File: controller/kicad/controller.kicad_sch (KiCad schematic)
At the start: 40 parts, among them J1 pcie_98, J2 USB_C_Receptacle_USB2.0, SW1 SW_MEC_5E, U1 WeAct_STM32H750_Module, U10 ESD5344D, U11 ESD5344D, U12 ESD5344D, U13 ESD5344D, U14 ESD5344D, U15 ESD5344D, U16 CP2102N-A01-GQFN28-Interface_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, U2 ESD5344D, U3 ESD5344D, U4 ESD5344D, U5 ESD5344D, U6 ESD5344D, U7 ESD5344D, U8 ESD5344D, U9 ESD5344D

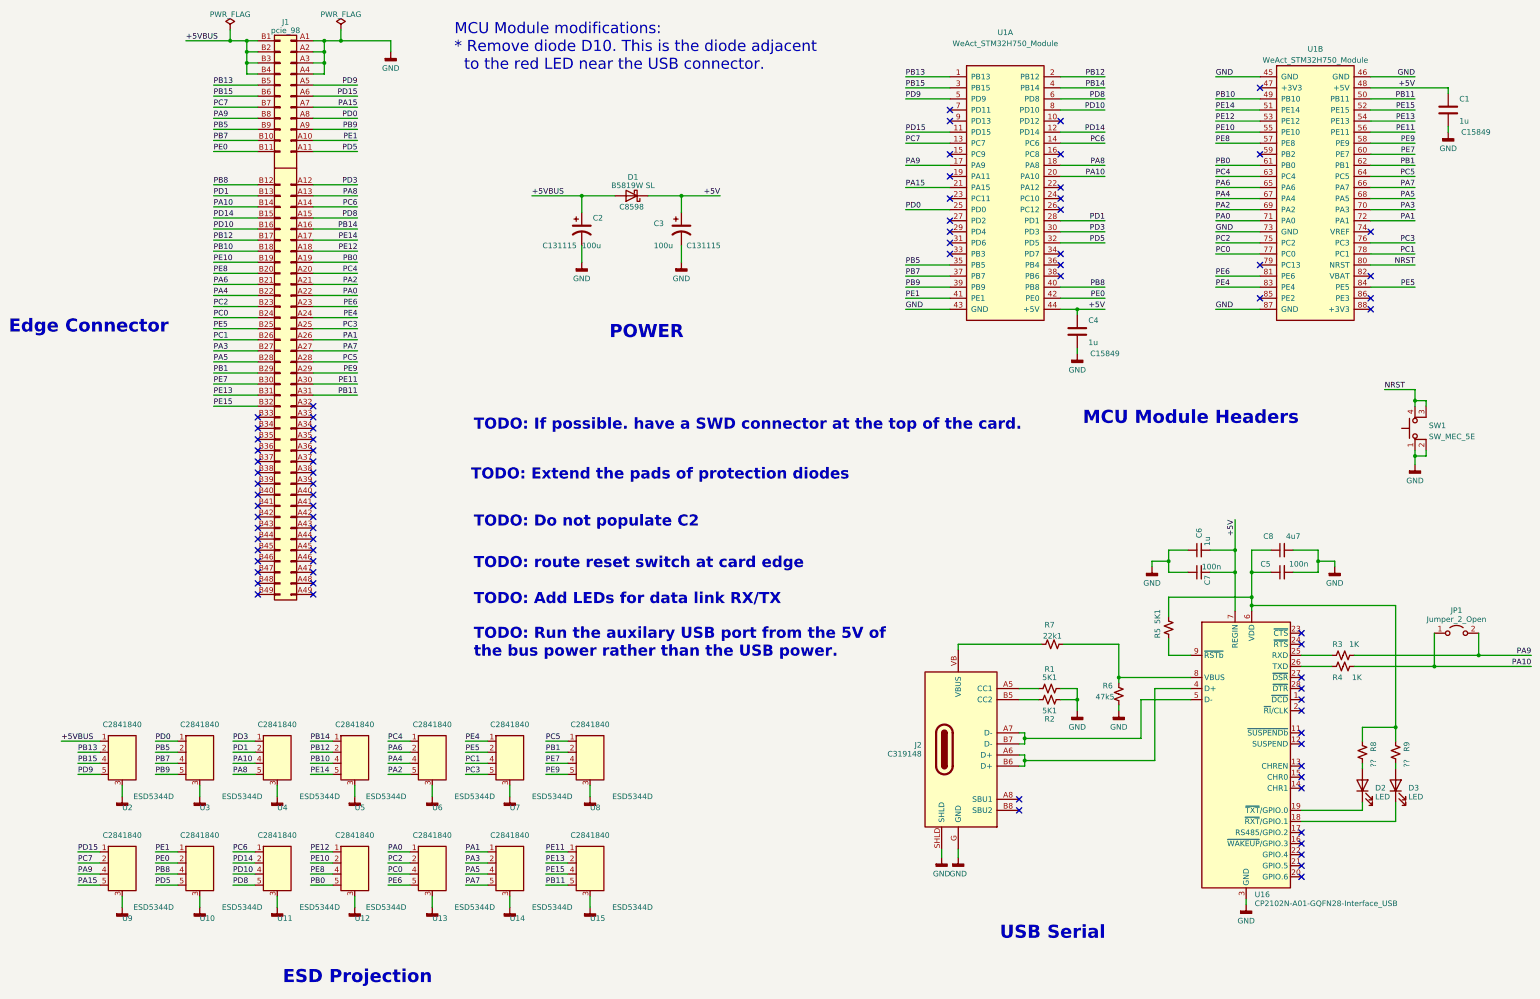
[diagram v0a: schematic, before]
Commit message: Cleaning up of the controller's PCB, in progress.
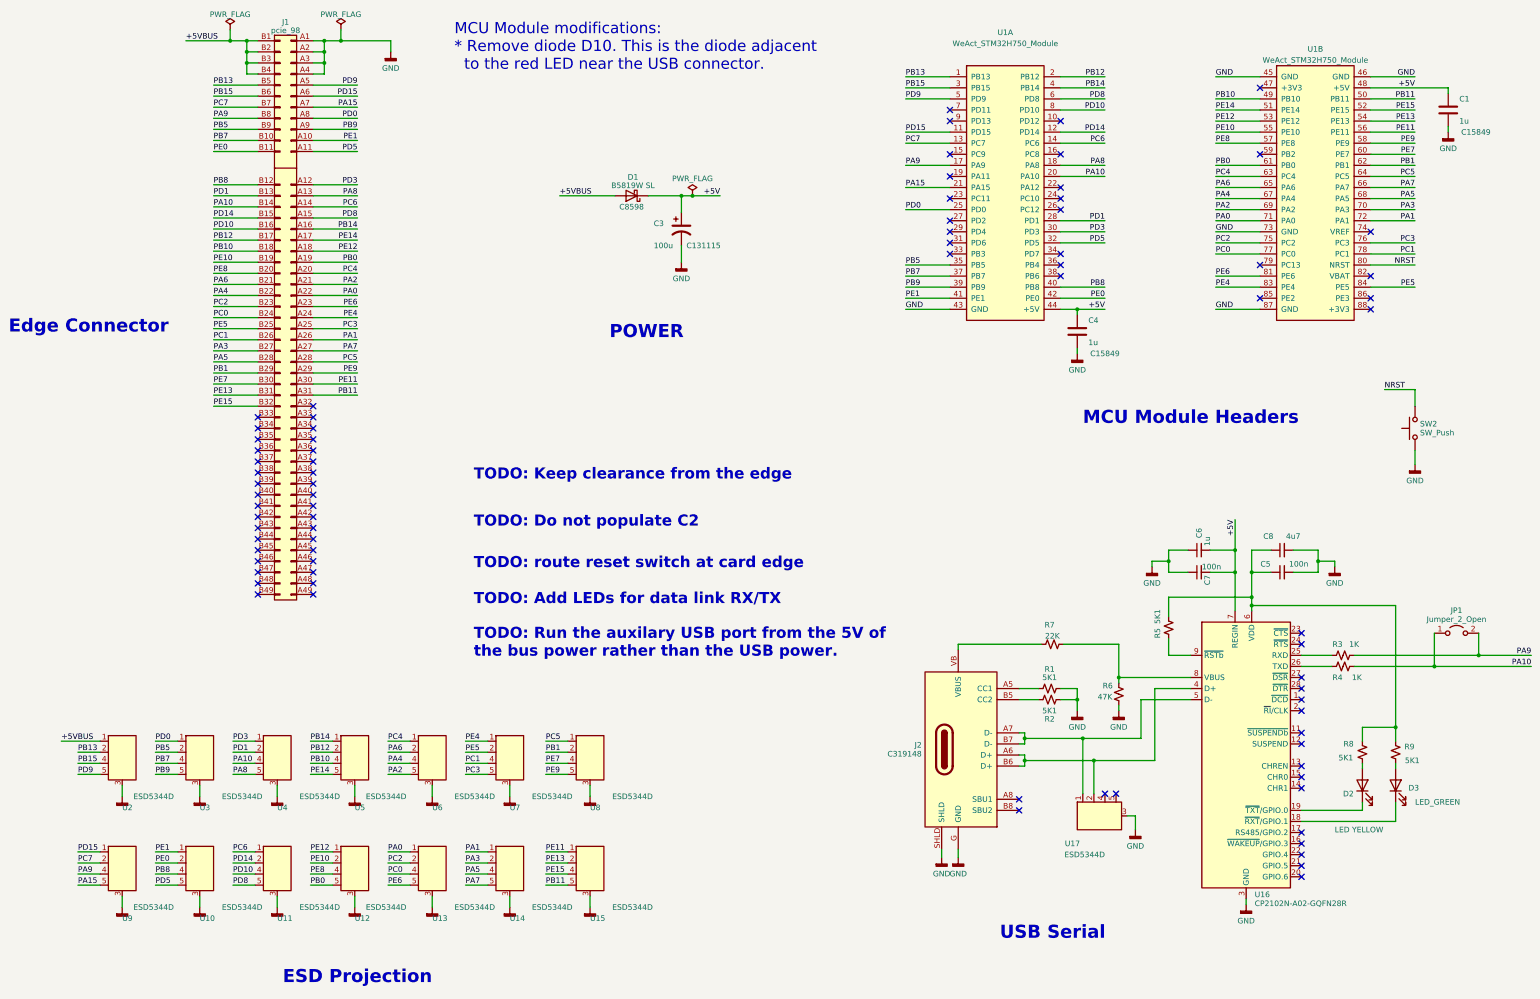
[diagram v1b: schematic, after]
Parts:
- removed C2: 100u, controller:CP_Elec_5x5.4_JLCPCB, symbol Device:C_Polarized_US
- removed SW1: SW_MEC_5E, symbol Switch:SW_MEC_5E
- added SW2: SW_Push, symbol Switch:SW_Push
- added U17: ESD5344D, common:Diodes_UDFN-10_1.0x2.5mm_P0.5mm, symbol common:ESD5344D
- D2: value LED -> LED YELLOW; footprint (none) -> LED_SMD:LED_0603_1608Metric; LCSC (none) -> C72038
- D3: value LED -> LED_GREEN; footprint (none) -> LED_SMD:LED_0603_1608Metric; LCSC (none) -> C72043
- R6: value 47k5 -> 47K; LCSC (none) -> C25819
- R7: value 22k1 -> 22K; LCSC (none) -> C31850
- R8, R9: value ?? -> 5K1; LCSC (none) -> C23186
- U16: value CP2102N-A01-GQFN28-Interface_USB -> CP2102N-A02-GQFN28R; LCSC C6568 -> C964632
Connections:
- net GND: now also SW2.1, U17.3 (GND)
- net NRST: now also SW2.2
- net at D2.2 (A): now also R8.1; no longer R8.2
- net at C5.1, C8.1, R5.2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: now also R8.2, R9.2; no longer R8.1, R9.1
- net at J2.A6 (D+), J2.B6 (D+), U16.4 (D+): now also U17.2 (D2)
- net at J2.A7 (D-), J2.B7 (D-), U16.5 (D-): now also U17.1 (D1)
- net at D3.2 (A): now also R9.1; no longer R9.2
- no-connect marks 78 -> 80
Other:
- note added: "TODO: Keep clearance from the edge"
- note removed: "TODO: Extend the pads of protection diodes"
- note removed: "TODO: If possible. have a SWD connector at the top of the card."

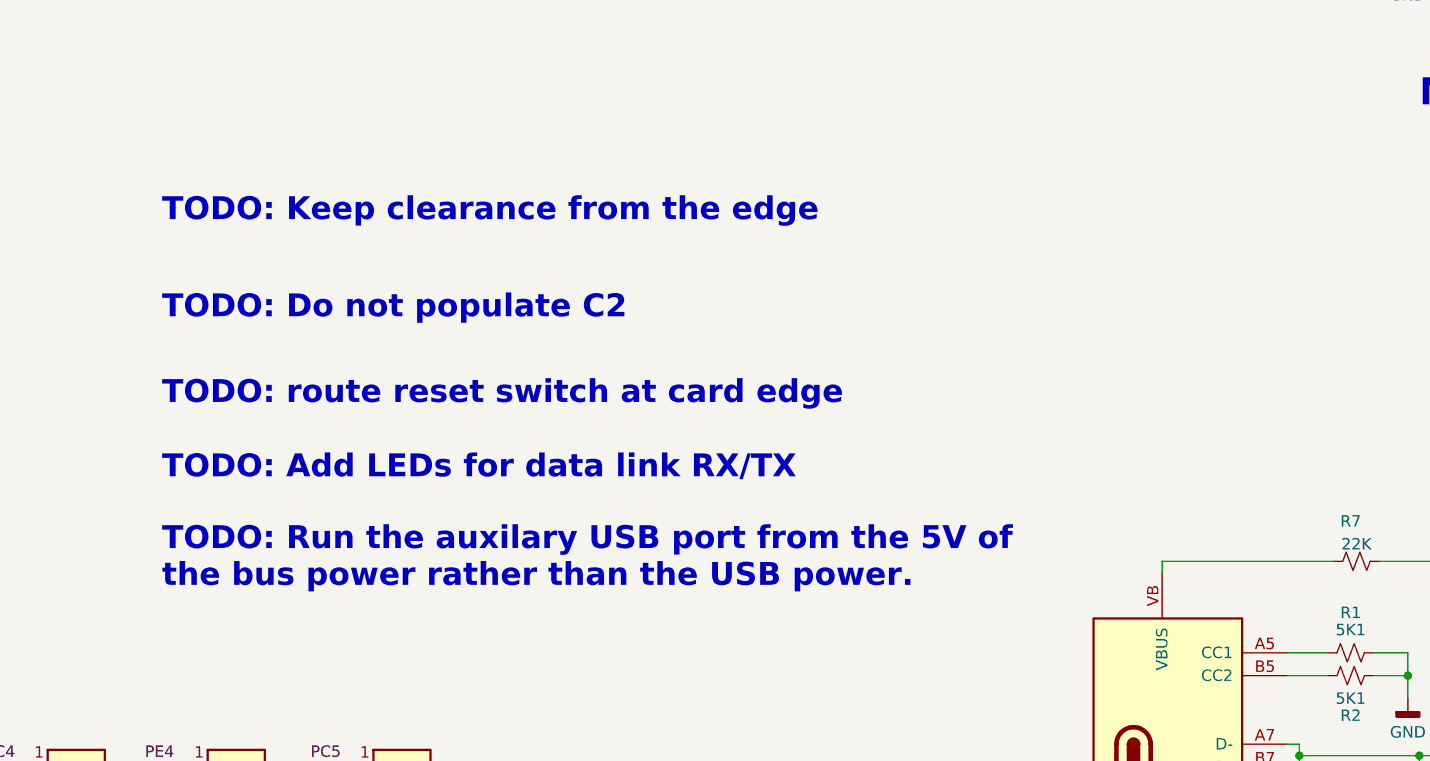
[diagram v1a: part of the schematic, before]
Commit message: Made the Controller PCB changes, per the schematic's TODOs.
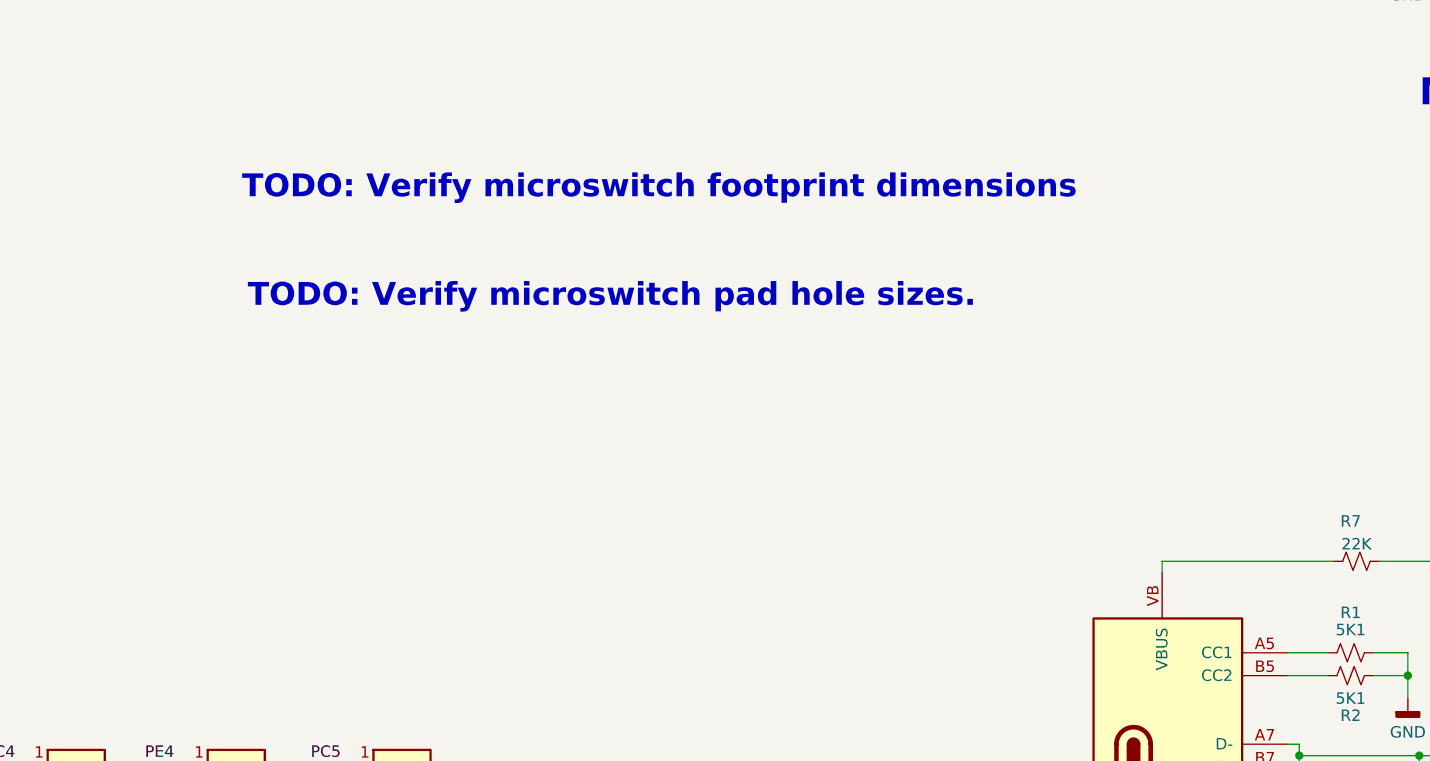
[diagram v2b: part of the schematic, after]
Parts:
- SW2: footprint (none) -> controller:microswitch; LCSC (none) -> C726013
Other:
- note added: "TODO: Verify microswitch footprint dimensions"
- note added: "TODO: Verify microswitch pad hole sizes."
- note removed: "TODO: Add LEDs for data link RX/TX"
- note removed: "TODO: Do not populate C2"
- note removed: "TODO: Keep clearance from the edge"
- note removed: "TODO: Run the auxilary USB port from the 5V of the bus power rather than the USB power."
- note removed: "TODO: route reset switch at card edge"
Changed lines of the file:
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@@
     (effects (font (size 3 3) (thickness 0.6) bold) (justify left bottom))
-  )
-  (text "TODO: Run the auxilary USB port from the 5V of\nthe bus power rather than the USB power."
-    (at 139.065 179.705 0)
-    (effects (font (size 2.54 2.54) (thickness 0.508) bold (color 255 0 0 1)) (justify left bottom))
   )
   (text "MCU Module Headers" (at 278.765 126.365 0)
@@
     (effects (font (size 3 3) (thickness 0.6) bold) (justify left bottom))
   )
-  (text "TODO: Keep clearance from the edge" (at 139.065 139.065 0)
-    (effects (font (size 2.54 2.54) (thickness 0.508) bold (color 255 0 0 1)) (justify left bottom))
-  )
-  (text "TODO: Add LEDs for data link RX/TX" (at 139.065 167.64 0)
-    (effects (font (size 2.54 2.54) (thickness 0.508) bold (color 255 0 0 1)) (justify left bottom))
-  )
   (text "Edge Connector" (at 32.385 105.41 0)
     (effects (font (size 3 3) (thickness 0.6) bold) (justify left bottom))
   )
-  (text "TODO: Do not populate C2" (at 139.065 149.86 0)
+  (text "TODO: Verify microswitch pad hole sizes." (at 148.59 148.59 0)
     (effects (font (size 2.54 2.54) (thickness 0.508) bold (color 255 0 0 1)) (justify left bottom))
   )
@@
     (effects (font (size 2.54 2.54)) (justify left bottom))
   )
-  (text "TODO: route reset switch at card edge" (at 139.065 159.385 0)
+  (text "TODO: Verify microswitch footprint dimensions\n" (at 147.955 136.525 0)
     (effects (font (size 2.54 2.54) (thickness 0.508) bold (color 255 0 0 1)) (justify left bottom))
   )
@@
       (effects (font (size 1.27 1.27)) (justify right))
     )
-    (property "Footprint" "" (at 349.885 127 0)
+    (property "Footprint" "controller:microswitch" (at 349.885 127 0)
       (effects (font (size 1.27 1.27)) hide)
     )
@@
       (effects (font (size 1.27 1.27)) hide)
     )
+    (property "LCSC" "C726013" (at 354.965 127 90)
+      (effects (font (size 1.27 1.27)) hide)
+    )

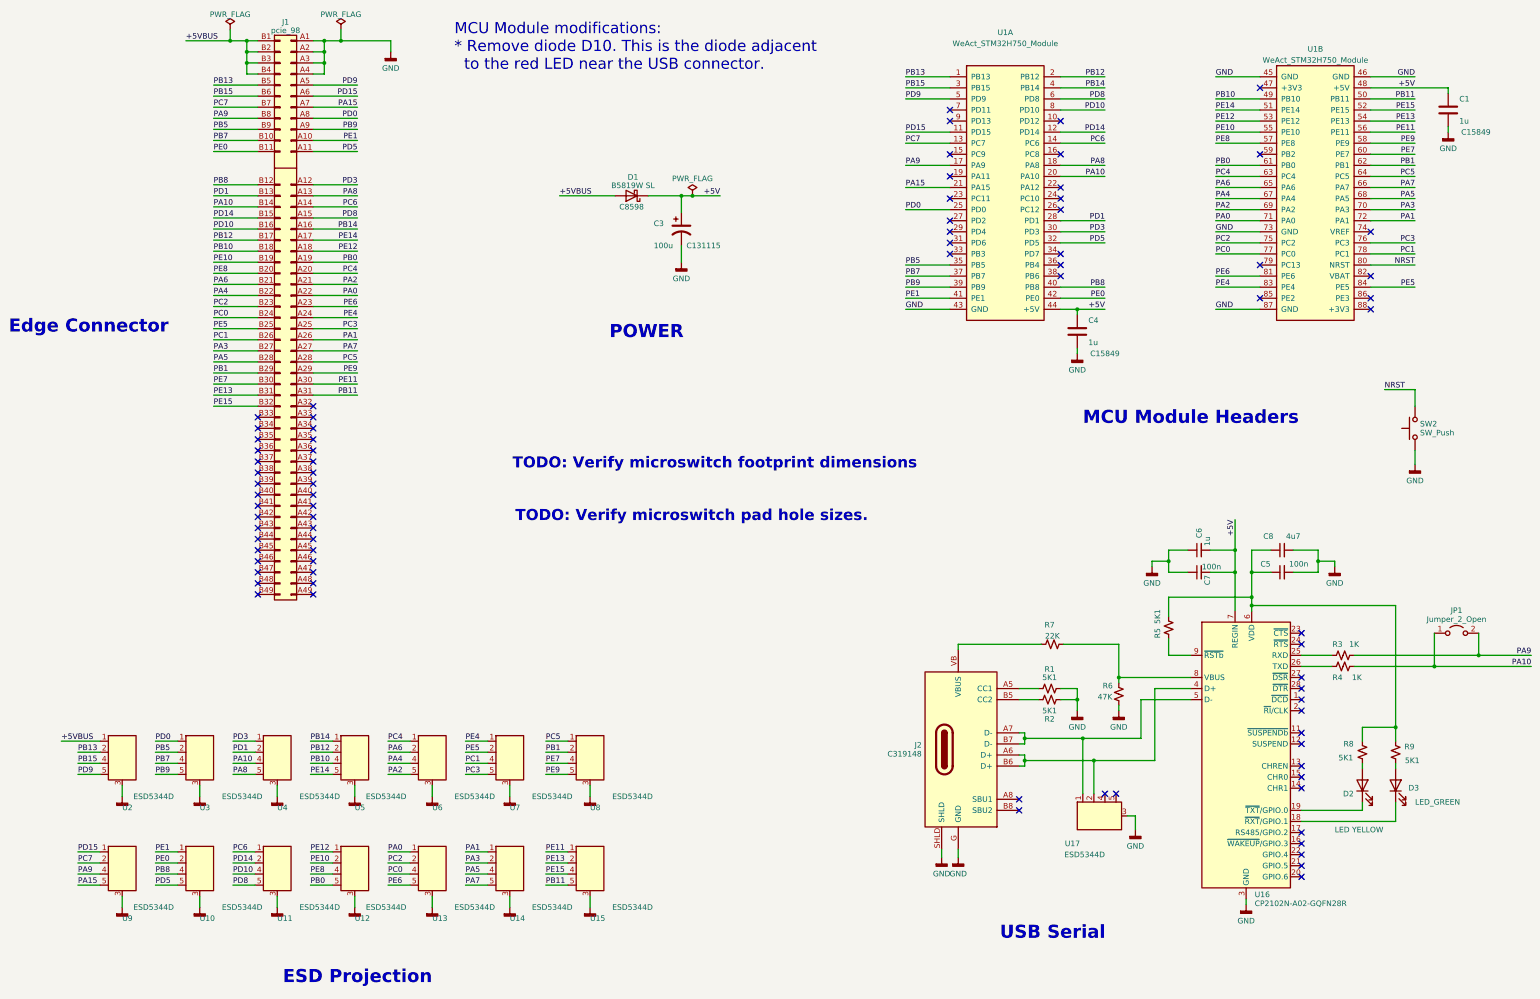
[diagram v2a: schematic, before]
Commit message: Verified and updated the microswitch footprint.
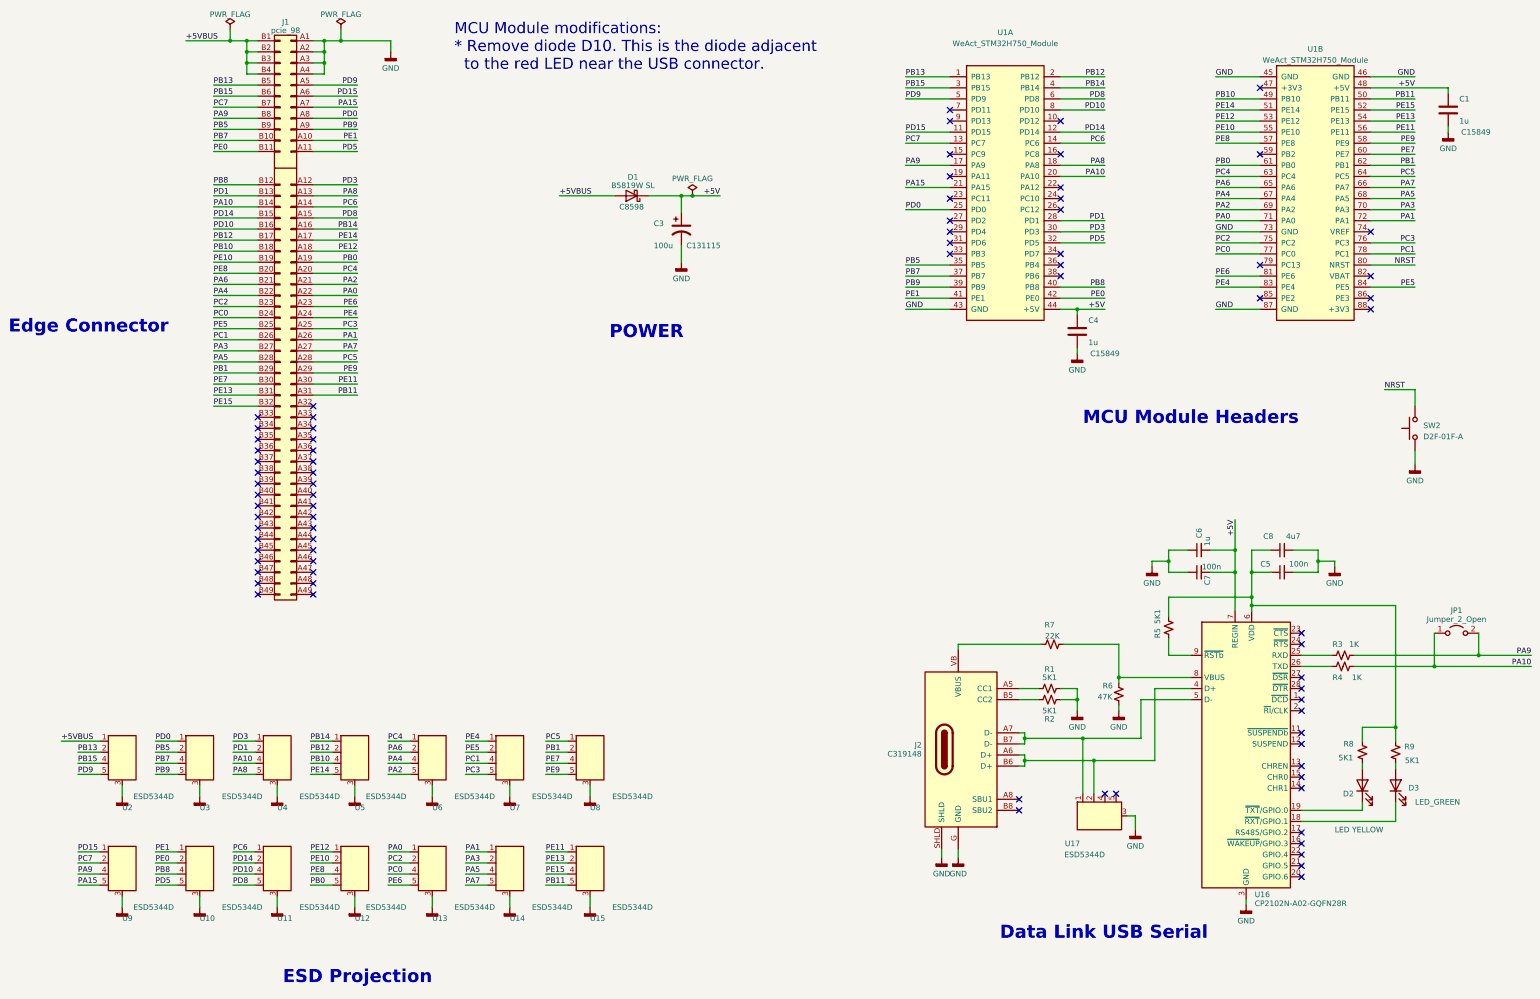
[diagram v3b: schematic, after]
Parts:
- SW2: value SW_Push -> D2F-01F-A
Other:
- note added: "Data Link USB Serial"
- note removed: "TODO: Verify microswitch footprint dimensions"
- note removed: "TODO: Verify microswitch pad hole sizes."
- note removed: "USB Serial"
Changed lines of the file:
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@@
     (effects (font (size 3 3) (thickness 0.6) bold) (justify left bottom))
   )
-  (text "USB Serial" (at 259.715 244.475 0)
+  (text "Data Link USB Serial" (at 259.715 244.475 0)
     (effects (font (size 3 3) (thickness 0.6) bold) (justify left bottom))
   )
   (text "Edge Connector" (at 32.385 105.41 0)
     (effects (font (size 3 3) (thickness 0.6) bold) (justify left bottom))
-  )
-  (text "TODO: Verify microswitch pad hole sizes." (at 148.59 148.59 0)
-    (effects (font (size 2.54 2.54) (thickness 0.508) bold (color 255 0 0 1)) (justify left bottom))
   )
   (text "POWER" (at 170.18 106.68 0)
@@
     (at 134.62 45.085 0)
     (effects (font (size 2.54 2.54)) (justify left bottom))
-  )
-  (text "TODO: Verify microswitch footprint dimensions\n" (at 147.955 136.525 0)
-    (effects (font (size 2.54 2.54) (thickness 0.508) bold (color 255 0 0 1)) (justify left bottom))
   )
   (label "PB11" (at 112.395 119.38 180) (fields_autoplaced)
@@
   (symbol (lib_id "Switch:SW_Push") (at 354.965 127 90) (unit 1)
     (in_bom yes) (on_board yes) (dnp no) (fields_autoplaced)
-    (property "Reference" "SW2" (at 356.108 125.976 90)
+    (property "Reference" "SW2" (at 356.87 126.365 90)
       (effects (font (size 1.27 1.27)) (justify right))
     )
-    (property "Value" "SW_Push" (at 356.108 128.024 90)
+    (property "Value" "D2F-01F-A\n" (at 356.87 128.905 90)
       (effects (font (size 1.27 1.27)) (justify right))
     )
